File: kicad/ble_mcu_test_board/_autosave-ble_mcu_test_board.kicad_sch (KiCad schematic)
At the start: 22 parts, among them J1 I2C, J2 SWD, U1 STM32WB10CCUx, U2 DLF162500LT-5028A1, Y1 32MHz

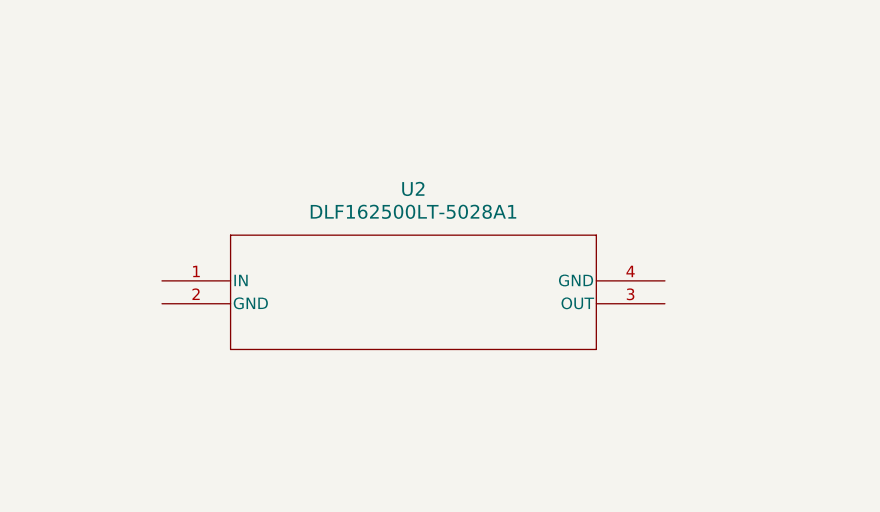
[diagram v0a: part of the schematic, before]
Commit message: modified schematic, added cubeide project, added symbol/footprint for filter chip
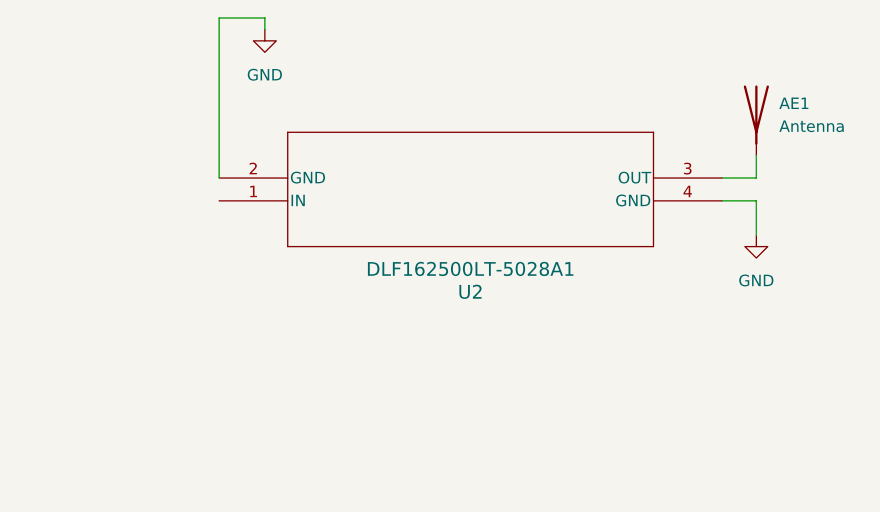
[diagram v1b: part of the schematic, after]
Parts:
- added AE1: Antenna, symbol Device:Antenna
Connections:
- net GND: now also U2.2 (GND), U2.4 (GND)
- net at U2.3 (OUT): now also AE1.1 (A)
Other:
- moved on the sheet: U2
